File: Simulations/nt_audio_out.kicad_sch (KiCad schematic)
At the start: 9 parts

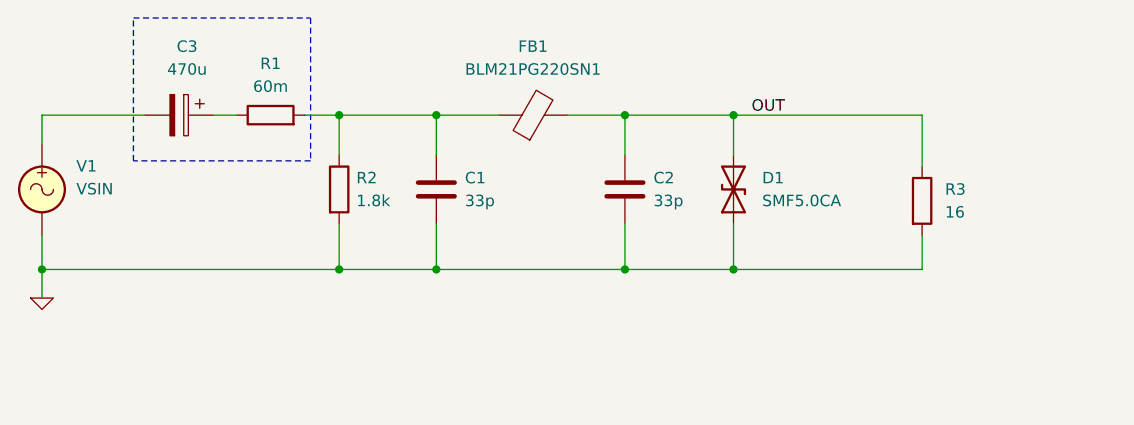
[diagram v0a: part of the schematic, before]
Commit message: switch power to 9V
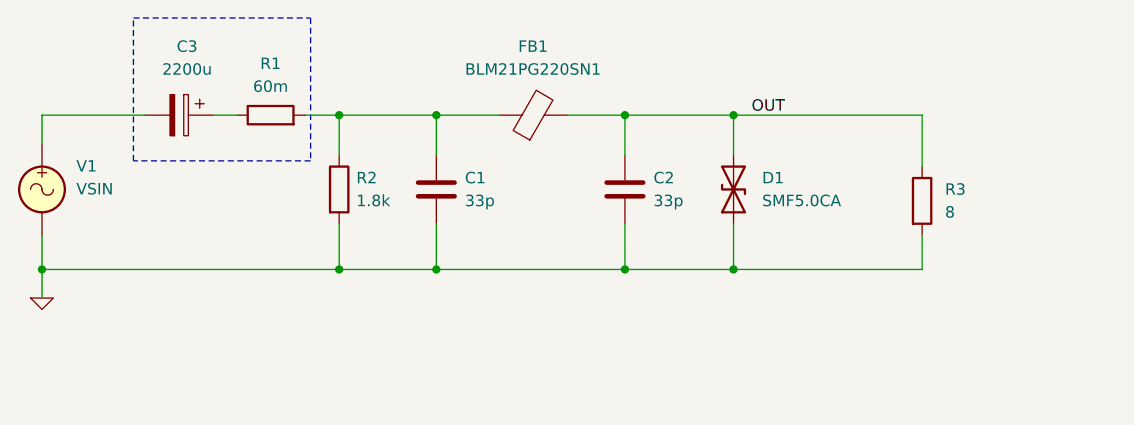
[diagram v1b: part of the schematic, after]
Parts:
- C3: value 470u -> 2200u
- R3: value 16 -> 8
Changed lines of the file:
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@@
     (pin "2")
     (instances
-      (project "nt_audio_out_freq"
+      (project "nt_audio_out"
         (path "/4dd0498c-4c77-4591-ad31-e443b8a6e20e"
           (reference "C2") (unit 1)
@@
       (effects (font (size 1.27 1.27)) (justify left))
     )
-    (property "Value" "16" (at 191.77 78.105 0)
+    (property "Value" "8" (at 191.77 78.105 0)
       (effects (font (size 1.27 1.27)) (justify left))
     )
@@
     (pin "2")
     (instances
-      (project "nt_audio_out_freq"
+      (project "nt_audio_out"
         (path "/4dd0498c-4c77-4591-ad31-e443b8a6e20e"
           (reference "R3") (unit 1)
@@
     (pin "2")
     (instances
-      (project "nt_audio_out_freq"
+      (project "nt_audio_out"
         (path "/4dd0498c-4c77-4591-ad31-e443b8a6e20e"
           (reference "D1") (unit 1)
@@
     (pin "1")
     (instances
-      (project "nt_audio_out_freq"
+      (project "nt_audio_out"
         (path "/4dd0498c-4c77-4591-ad31-e443b8a6e20e"
           (reference "#GND01") (unit 1)
@@
     (pin "2")
     (instances
-      (project "nt_audio_out_freq"
+      (project "nt_audio_out"
         (path "/4dd0498c-4c77-4591-ad31-e443b8a6e20e"
           (reference "V1") (unit 1)
@@
     (pin "2")
     (instances
-      (project "nt_audio_out_freq"
+      (project "nt_audio_out"
         (path "/4dd0498c-4c77-4591-ad31-e443b8a6e20e"
           (reference "C1") (unit 1)
@@
       (effects (font (size 1.27 1.27)))
     )
-    (property "Value" "470u" (at 107.569 62.23 90)
+    (property "Value" "2200u" (at 107.569 62.23 90)
       (effects (font (size 1.27 1.27)))
     )
@@
     (pin "2")
     (instances
-      (project "nt_audio_out_freq"
+      (project "nt_audio_out"
         (path "/4dd0498c-4c77-4591-ad31-e443b8a6e20e"
           (reference "C3") (unit 1)
@@
     (pin "2")
     (instances
-      (project "nt_audio_out_freq"
+      (project "nt_audio_out"
         (path "/4dd0498c-4c77-4591-ad31-e443b8a6e20e"
           (reference "R1") (unit 1)
@@
     (pin "2")
     (instances
-      (project "nt_audio_out_freq"
+      (project "nt_audio_out"
         (path "/4dd0498c-4c77-4591-ad31-e443b8a6e20e"
           (reference "FB1") (unit 1)
@@
     (pin "2")
     (instances
-      (project "nt_audio_out_freq"
+      (project "nt_audio_out"
         (path "/4dd0498c-4c77-4591-ad31-e443b8a6e20e"
           (reference "R2") (unit 1)
